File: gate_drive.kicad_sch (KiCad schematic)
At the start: 115 parts, among them M1A1 HIGHCURRENTPAD2, M1B1 HIGHCURRENTPAD2, M1C1 HIGHCURRENTPAD2, M2A1 HIGHCURRENTPAD2, M2B1 HIGHCURRENTPAD2, M2C1 HIGHCURRENTPAD2, U1 EG2131, U2 EG2131, U3 LM358, U4 EG2131, U5 EG2131, U6 LM358, U7 EG2131, U8 EG2131

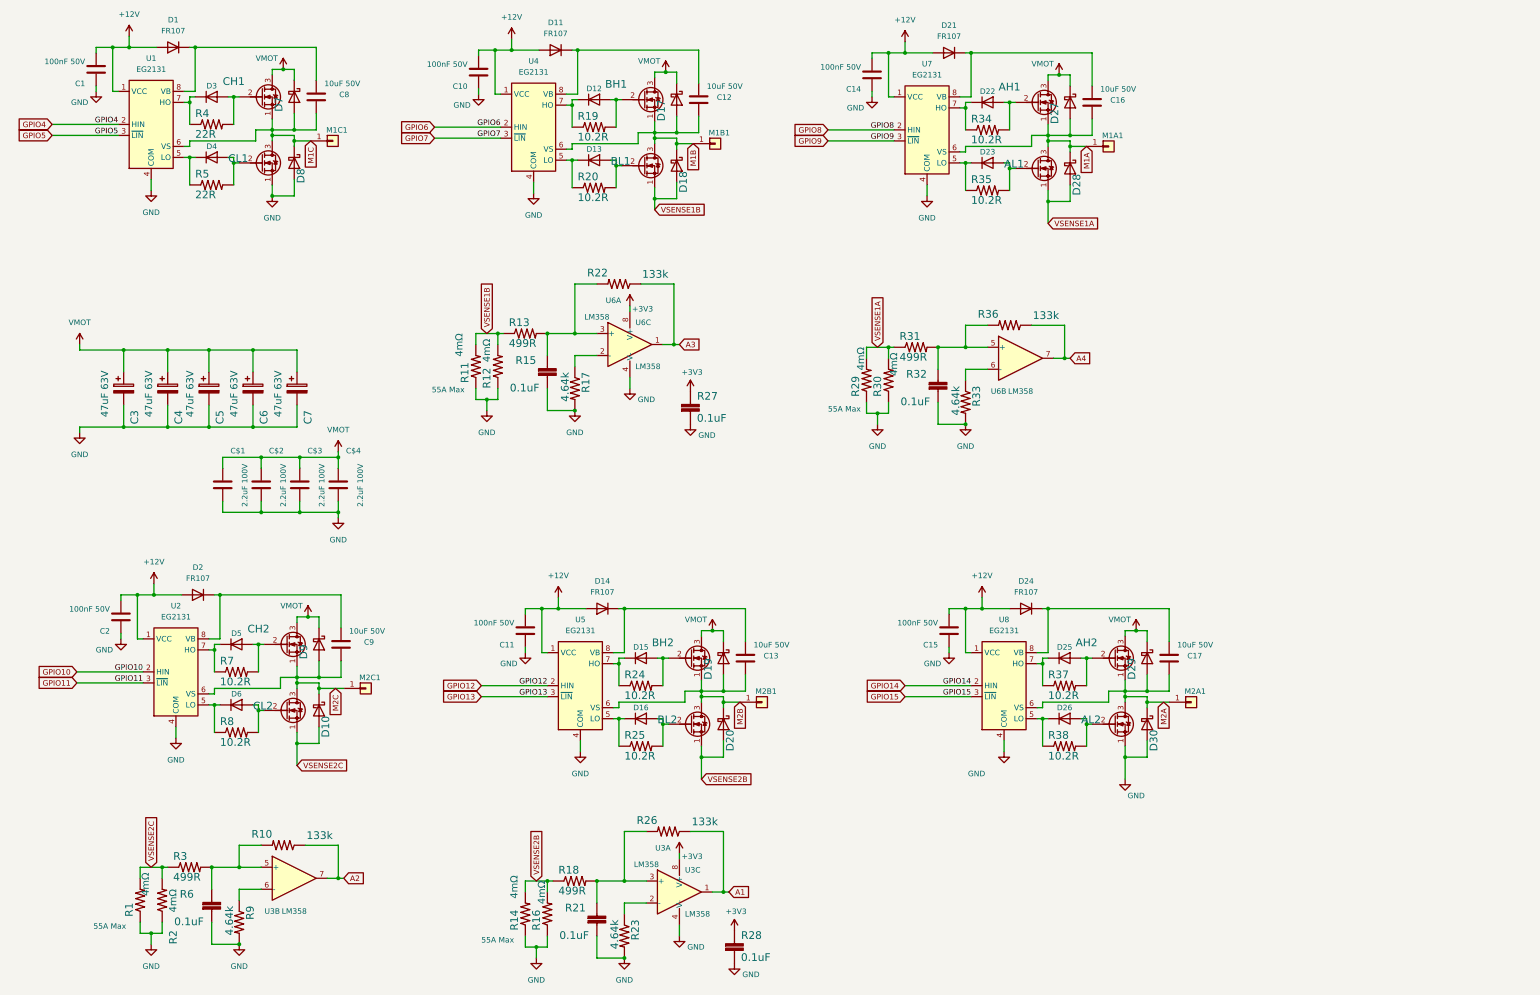
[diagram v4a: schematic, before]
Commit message: updated design with dual CPUs
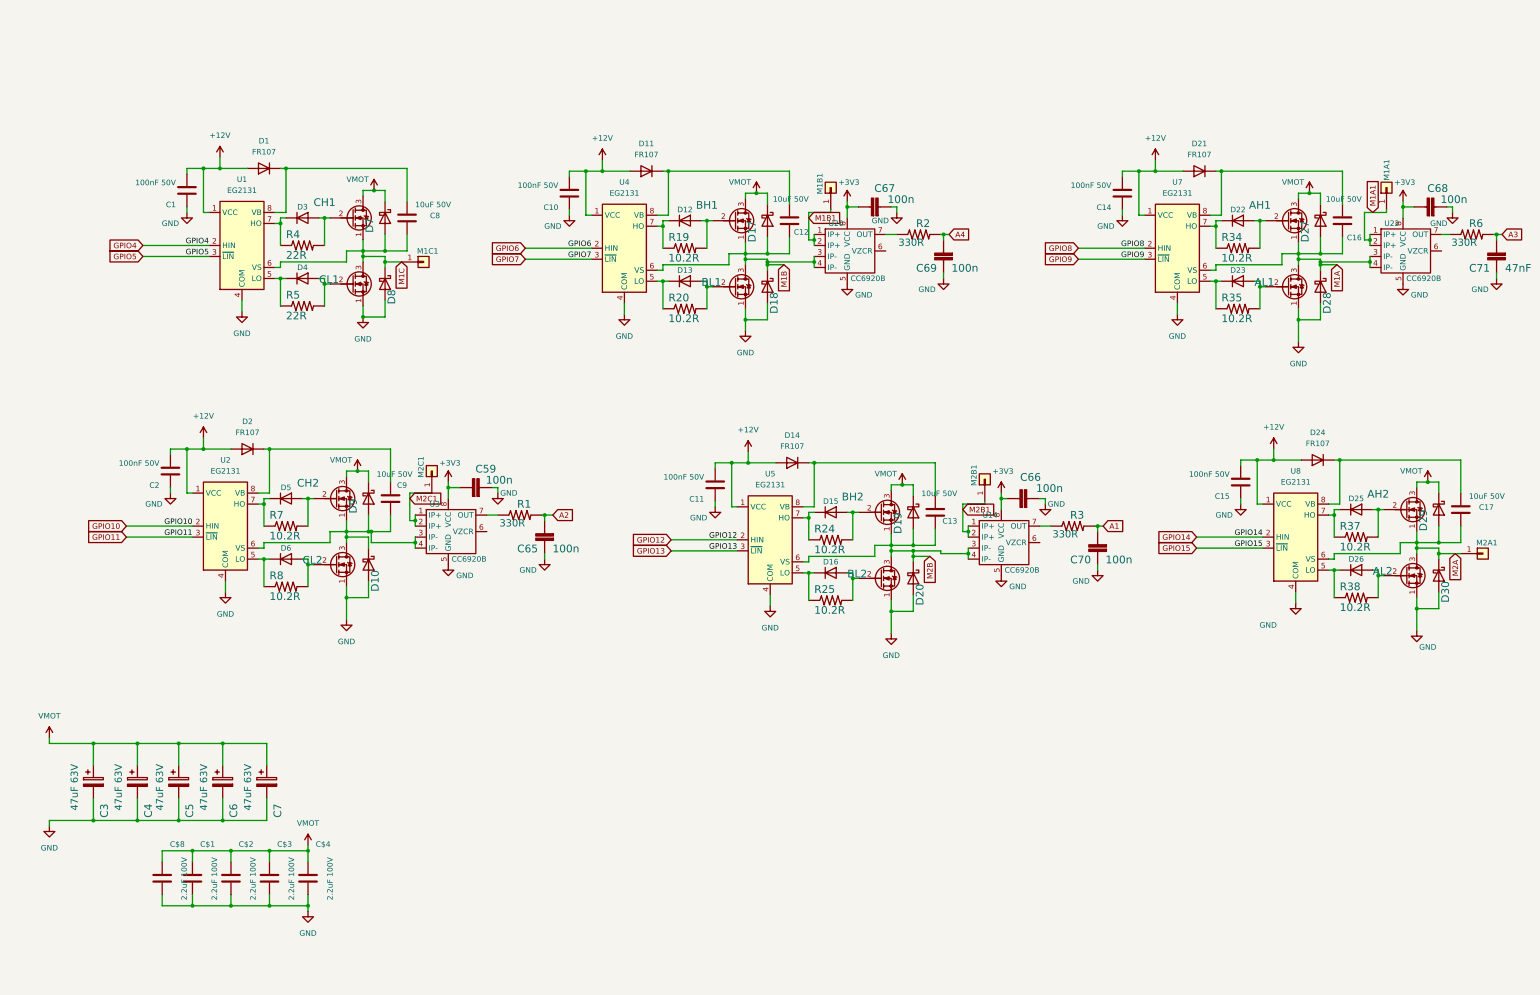
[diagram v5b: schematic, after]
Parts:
- removed R10, R22, R26, R36: 133k, Resistor_SMD:R_0603_1608Metric, symbol MotorController:TAYLOR_RESISTOR
- removed R11, R12, R14, R16, R29, R30: 4mΩ, Resistor_SMD:R_2512_6332Metric, symbol MotorController:TAYLOR_RESISTOR
- removed R13, R18, R31: 499R, Resistor_SMD:R_0603_1608Metric, symbol MotorController:TAYLOR_RESISTOR
- removed R15, R21, R27, R28, R32, R6: 0.1uF, Capacitor_SMD:C_0603_1608Metric, symbol MotorController:SPARKFUN-CAPACITORS_CAP
- removed R17, R23, R33, R9: 4.64k, Resistor_SMD:R_0603_1608Metric, symbol MotorController:TAYLOR_RESISTOR
- removed U3, U6: LM358, Package_SO:MSOP-8_3x3mm_P0.65mm, symbol Amplifier_Operational:LM358
- added C$8: 2.2uF 100V, Capacitor_SMD:C_1206_3216Metric, symbol Device:C
- added C59, C65, C66, C67, C68, C69, C70: 100n, Capacitor_SMD:C_0603_1608Metric, symbol MotorController:SPARKFUN-CAPACITORS_CAP
- added C71: 47nF, Capacitor_SMD:C_0603_1608Metric, symbol MotorController:SPARKFUN-CAPACITORS_CAP
- added R6: 330R, Resistor_SMD:R_0603_1608Metric, symbol MotorController:TAYLOR_RESISTOR
- added U14, U20, U22, U3: CC6920B, Package_SO:SOIC-8_3.9x4.9mm_P1.27mm, symbol motor_parts:CC6920B
- R1, R2: value 4mΩ -> 330R; footprint Resistor_SMD:R_2512_6332Metric -> Resistor_SMD:R_0603_1608Metric; LCSC C375693 -> C105881
- R3: value 499R -> 330R; LCSC C101076 -> C105881
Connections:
- net VSENSE1A is gone; now on net GND: AL1.1 (S), D28.2 (A)
- net VSENSE1B is gone; now on net GND: BL1.1 (S), D18.2 (A)
- net VSENSE2B is gone; now on net GND: BL2.1 (S), D20.2 (A)
- net +3V3: now also C59.1, C66.1, C67.1, C68.1, U14.8 (VCC), U20.8 (VCC), U22.8 (VCC), U3.8 (VCC)
- net A1: now also R3.2, C70.2
- net A2: now also R1.2, C65.2
- net A3: now also C71.2, R6.2
- net A4: now also R2.2, C69.2
- net GND: now also CL2.1 (S), D10.2 (A), C$8.2, C59.2, C65.1, C66.2, C67.2, C68.2, C69.1, C70.1, C71.1, U14.5 (GND), U20.5 (GND), U22.5 (GND), U3.5 (GND); no longer R1.1, R2.1
- net M1A: now also U22.3 (IP-), U22.4 (IP-); no longer M1A1.1 (Pin_1)
- net M1B: now also U20.3 (IP-), U20.4 (IP-); no longer M1B1.1 (Pin_1)
- net M2B: now also U14.3 (IP-), U14.4 (IP-); no longer M2B1.1 (Pin_1)
- net VMOT: now also C$8.1
- net M2C: no longer names the net of C9.1, CH2.1 (S), CL2.3 (D), D10.1 (K), D9.2 (A), U2.6 (VS)
- net M2C: now also U3.3 (IP-), U3.4 (IP-); no longer M2C1.1 (Pin_1)
- removed net VSENSE2C: CL2.1 (S), D10.2 (A), R1.2, R2.2, R3.1
- new net: R2.1, U20.7 (OUT)
- new net: R1.1, U3.7 (OUT)
- new net: R3.1, U14.7 (OUT)
- new net: R6.1, U22.7 (OUT)
- new net M1A1: M1A1.1 (Pin_1), U22.1 (IP+), U22.2 (IP+)
- new net M1B1: M1B1.1 (Pin_1), U20.1 (IP+), U20.2 (IP+)
- new net M2B1: M2B1.1 (Pin_1), U14.1 (IP+), U14.2 (IP+)
- new net M2C1: M2C1.1 (Pin_1), U3.1 (IP+), U3.2 (IP+)
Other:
- note removed: "55A Max"
- moved on the sheet: AH1, AH2, AL1, AL2, BH1, BH2, BL1, BL2, C$1, C$2, C$3, C$4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

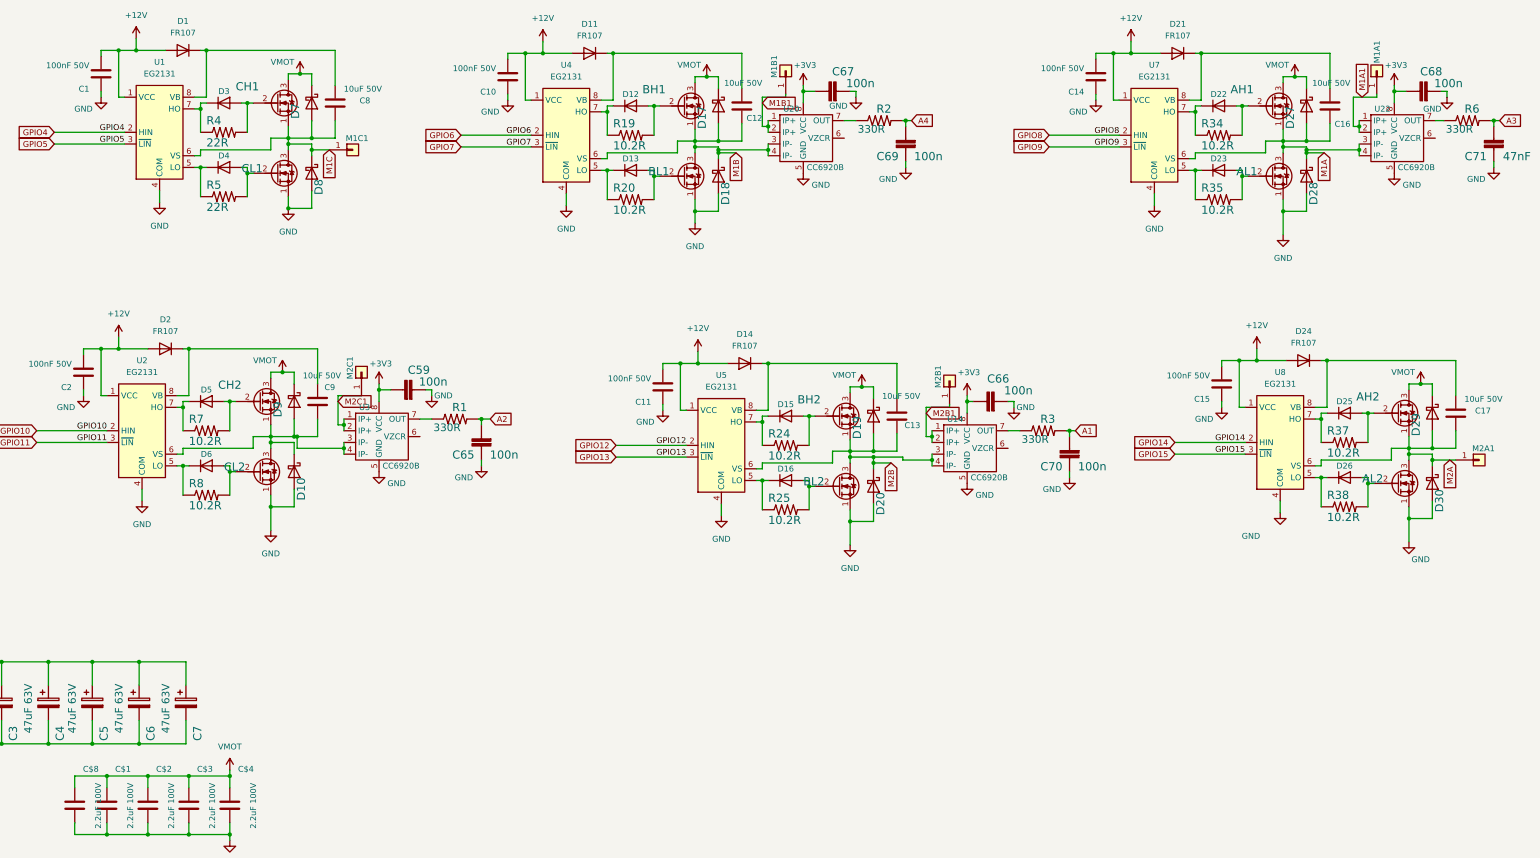
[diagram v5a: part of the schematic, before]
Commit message: Updated design with Dual CPUs and improved current measurement
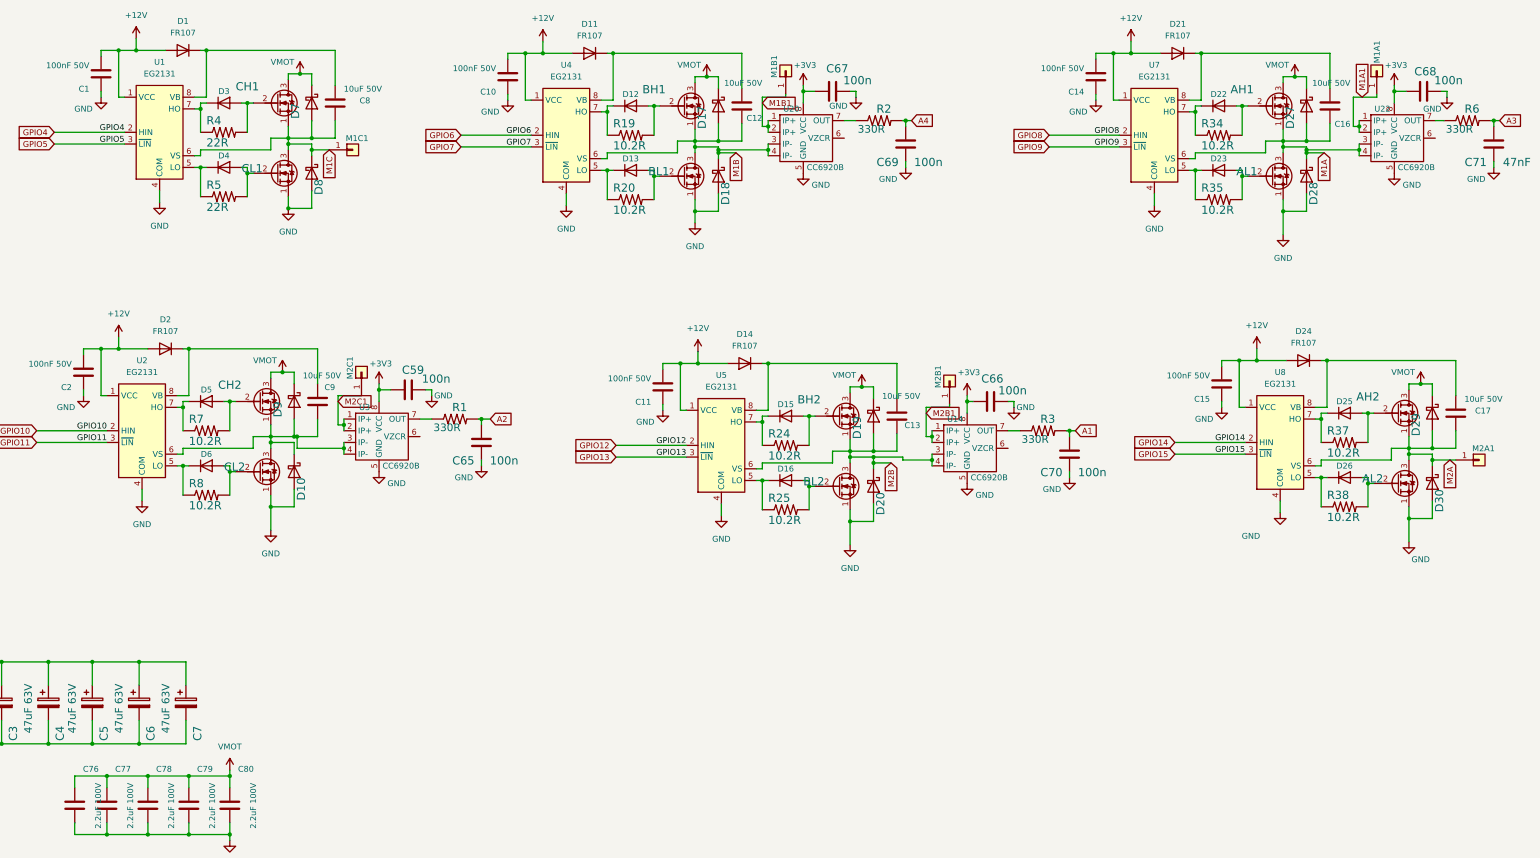
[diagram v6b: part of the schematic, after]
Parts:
- AH1, AH2, AL1, AL2, BH1, BH2, BL1, BL2, CH1, CH2, CL1, CL2: LCSC C180959 -> C2908526
- C59, C65, C66, C67, C68, C69, C70, C71: symbol MotorController:SPARKFUN-CAPACITORS_CAP -> Device:C
- U14, U20, U22, U3: LCSC (none) -> C2880435
- renumbered C$8 to C76, C$1 to C77, C$2 to C78, C$3 to C79, C$4 to C80

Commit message: Design that went to fab. Update controller design per design review.
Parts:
- added C82, C83, C84, C85: DNP, Capacitor_SMD:C_0402_1005Metric, symbol Device:C
- C59, C66, C67, C68: LCSC (none) -> C14663
- C65, C69, C70: value 100n -> 47n; LCSC (none) -> C1622
- U14, U20, U22, U3: LCSC C2880435 -> C2880436
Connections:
- net GND: now also C82.1, C83.1, C84.1, C85.1
- net at U20.6 (VZCR): now also C83.2
- net at U14.6 (VZCR): now also C84.2
- net at U3.6 (VZCR): now also C82.2
- net at U22.6 (VZCR): now also C85.2
